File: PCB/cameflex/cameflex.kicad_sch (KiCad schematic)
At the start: 44 parts, among them J1 ESP32-C3_Left, J2 ESP32-C3_Right, J3 CON5_HALL, Q1 JY317P, Q2 JY2605, Q3 JY2605, Q4 JY2605, U1 JY01(8559), U3 JY213L

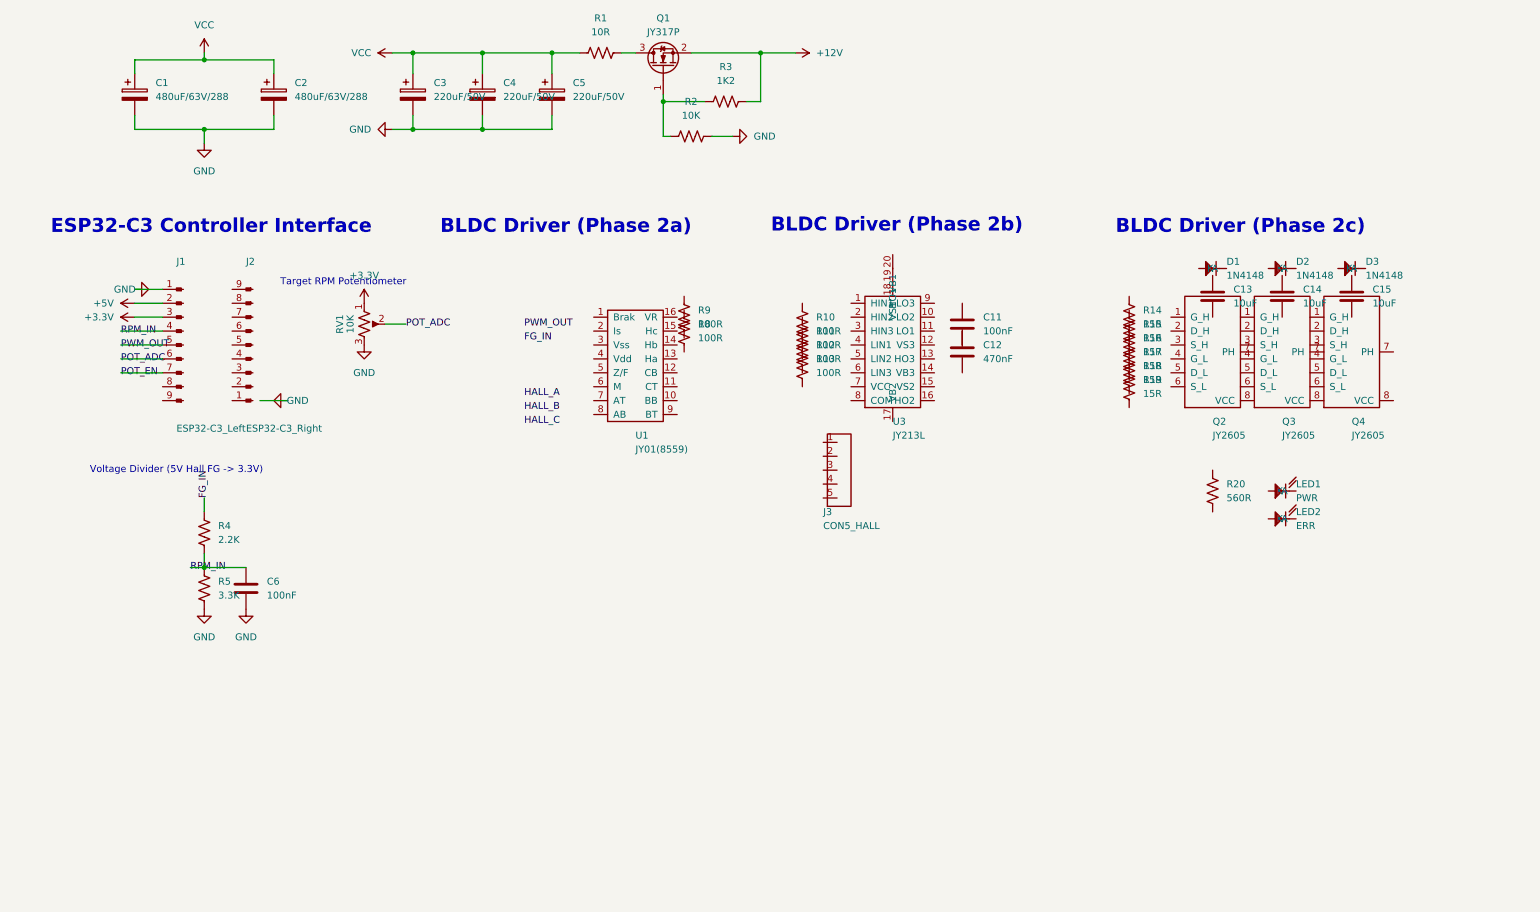
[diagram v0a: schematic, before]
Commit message: Chore: sync PCB cache and cleanup archived tuning assets
- Update .gitignore (note.txt, memory.db-*)
- Sync KiCad fp-info-cache and schematic/pcb whitespace
- Remove archived auto_tune bundle (superseded by current control)

Co-authored-by: Mema <mema@glassgallery.my.id>
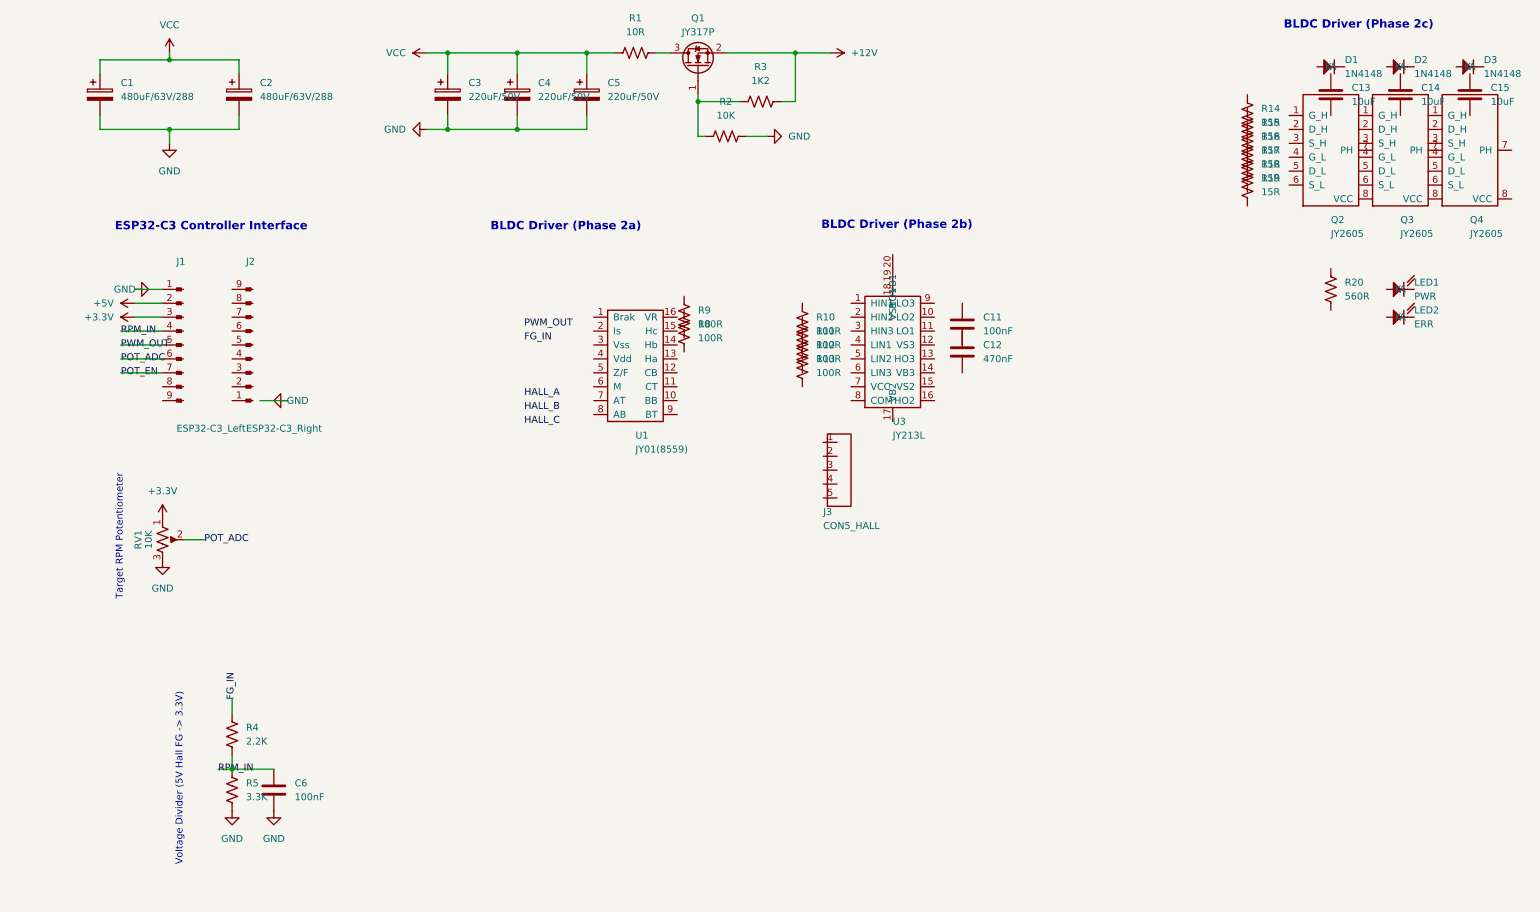
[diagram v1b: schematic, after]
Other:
- moved on the sheet: C1, C13, C14, C15, C2, C3, C4, C5, C6, D1, D2, D3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
